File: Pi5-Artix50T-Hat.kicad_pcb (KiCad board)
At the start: 4 copper layers, 65 x 56 mm, 97 parts, among them J1 GPIO, J2 Molex 0878321420, J3 68711614522, U1 FT24C256A, U10 AP62200TWU-7, U11 AP62200TWU-7, U12 AP62200TWU-7, U2 XC7A50T-FGG484, U9 AP62200TWU-7, X1 50MHz

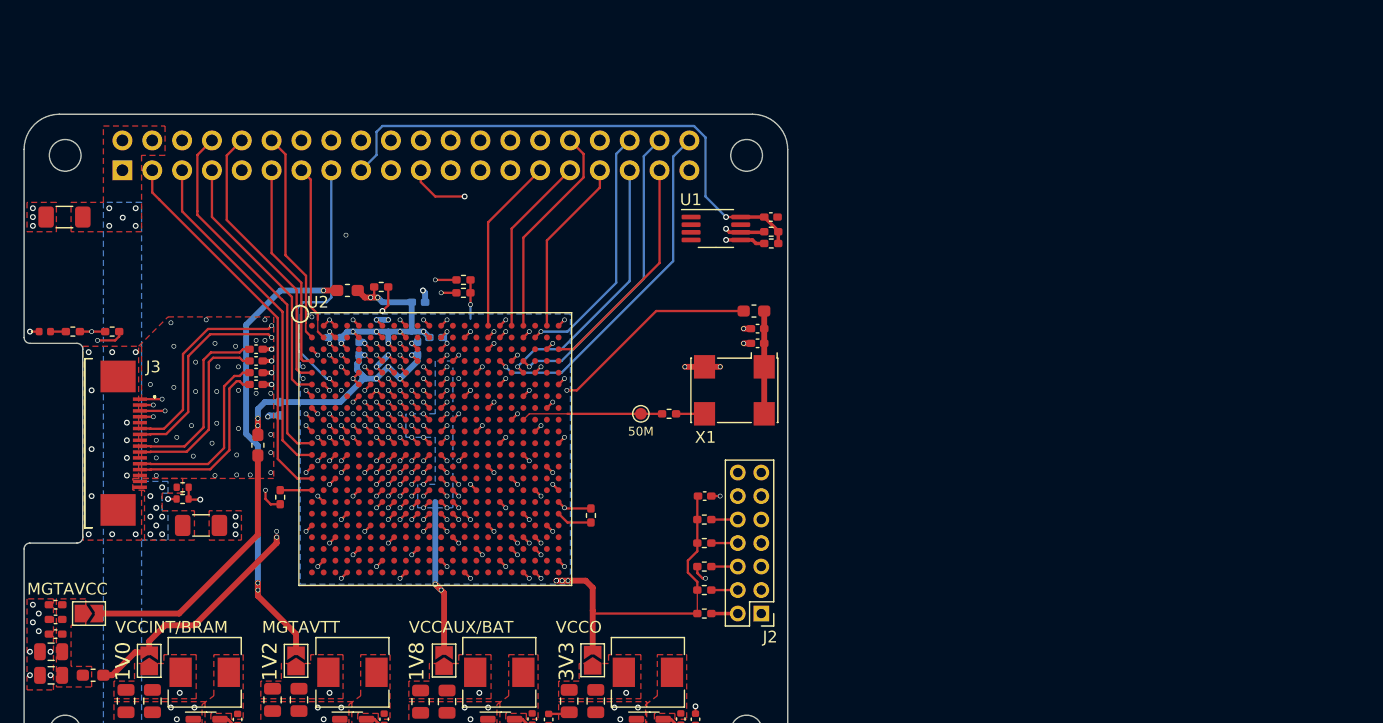
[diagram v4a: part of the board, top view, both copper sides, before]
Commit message: Updated decoupling. Need to work out larger planes and fills.
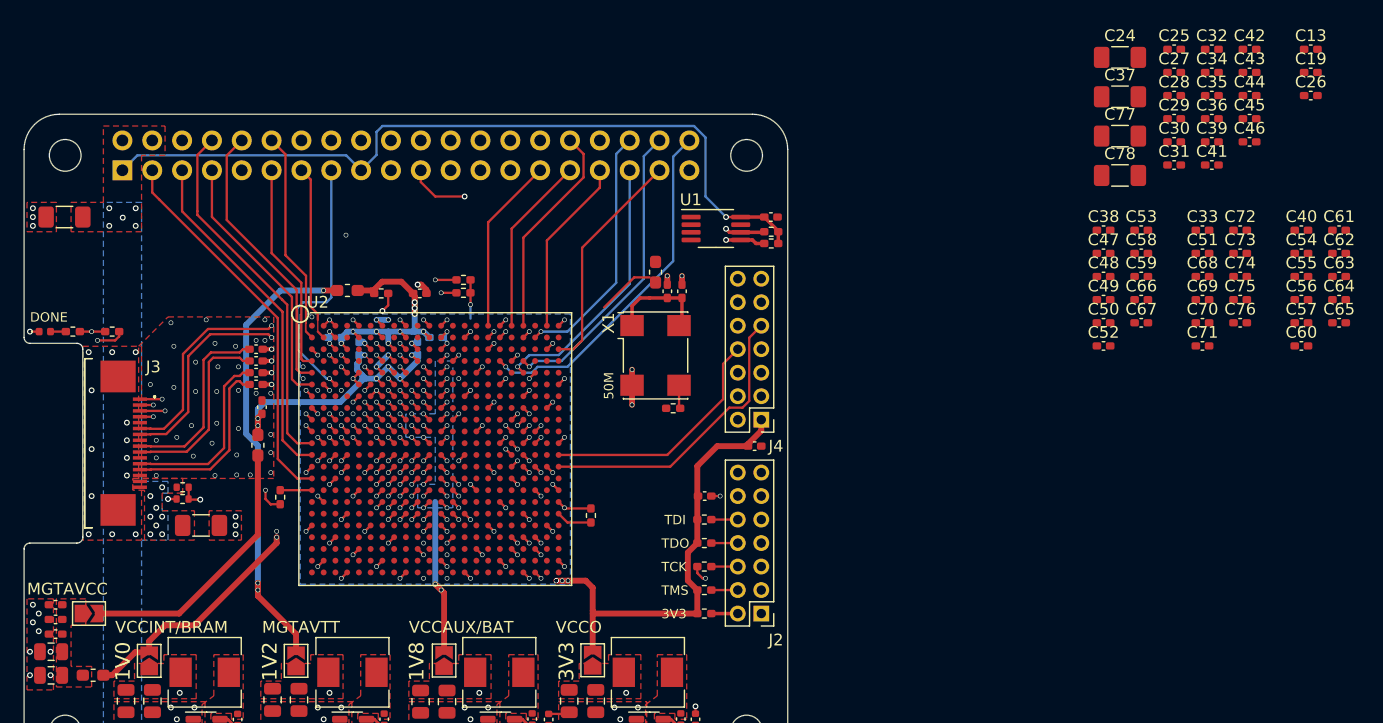
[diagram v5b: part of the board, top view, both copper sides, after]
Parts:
- removed TP1: 50M, TestPoint:TestPoint_Pad_D1.0mm
- added C13: 100n, Capacitor_SMD:C_0402_1005Metric_Pad0.74x0.62mm_HandSolder, F.Cu at (209.5, 38.5)
- added C19: 100n, Capacitor_SMD:C_0402_1005Metric_Pad0.74x0.62mm_HandSolder, F.Cu at (209.5, 40.4)
- added C22: 100n, Capacitor_SMD:C_0402_1005Metric_Pad0.74x0.62mm_HandSolder, F.Cu at (162.2, 72.2)
- added C24: 100u, Capacitor_SMD:C_1206_3216Metric_Pad1.33x1.80mm_HandSolder, F.Cu at (193.3, 39.2)
- added C25: 4.7u, Capacitor_SMD:C_0402_1005Metric_Pad0.74x0.62mm_HandSolder, F.Cu at (197.9, 38.5)
- added C26: 4.7u, Capacitor_SMD:C_0402_1005Metric_Pad0.74x0.62mm_HandSolder, F.Cu at (209.5, 42.4)
- added C27: 4.7u, Capacitor_SMD:C_0402_1005Metric_Pad0.74x0.62mm_HandSolder, F.Cu at (197.9, 40.4)
- added C28: 4.7u, Capacitor_SMD:C_0402_1005Metric_Pad0.74x0.62mm_HandSolder, F.Cu at (197.9, 42.4)
- added C29: 100n, Capacitor_SMD:C_0402_1005Metric_Pad0.74x0.62mm_HandSolder, F.Cu at (197.9, 44.4)
- added C30: 100n, Capacitor_SMD:C_0402_1005Metric_Pad0.74x0.62mm_HandSolder, F.Cu at (197.9, 46.4)
- added C31: 100n, Capacitor_SMD:C_0402_1005Metric_Pad0.74x0.62mm_HandSolder, F.Cu at (197.9, 48.3)
- added C32: 100n, Capacitor_SMD:C_0402_1005Metric_Pad0.74x0.62mm_HandSolder, F.Cu at (201.1, 38.5)
- added C33: 100n, Capacitor_SMD:C_0402_1005Metric_Pad0.74x0.62mm_HandSolder, F.Cu at (200.3, 53.9)
- added C34: 100n, Capacitor_SMD:C_0402_1005Metric_Pad0.74x0.62mm_HandSolder, F.Cu at (201.1, 40.4)
- added C35: 4.7u, Capacitor_SMD:C_0402_1005Metric_Pad0.74x0.62mm_HandSolder, F.Cu at (201.1, 42.4)
- added C36: 100n, Capacitor_SMD:C_0402_1005Metric_Pad0.74x0.62mm_HandSolder, F.Cu at (201.1, 44.4)
- added C37: 100u, Capacitor_SMD:C_1206_3216Metric_Pad1.33x1.80mm_HandSolder, F.Cu at (193.3, 42.5)
- added C38: 100n, Capacitor_SMD:C_0402_1005Metric_Pad0.74x0.62mm_HandSolder, F.Cu at (191.9, 53.9)
- added C39: 4.7u, Capacitor_SMD:C_0402_1005Metric_Pad0.74x0.62mm_HandSolder, F.Cu at (201.1, 46.4)
- added C40: 100n, Capacitor_SMD:C_0402_1005Metric_Pad0.74x0.62mm_HandSolder, F.Cu at (208.7, 53.9)
- added C41: 4.7u, Capacitor_SMD:C_0402_1005Metric_Pad0.74x0.62mm_HandSolder, F.Cu at (201.1, 48.3)
- added C42: 100n, Capacitor_SMD:C_0402_1005Metric_Pad0.74x0.62mm_HandSolder, F.Cu at (204.3, 38.5)
- added C43: 100n, Capacitor_SMD:C_0402_1005Metric_Pad0.74x0.62mm_HandSolder, F.Cu at (204.3, 40.4)
- added C44: 100n, Capacitor_SMD:C_0402_1005Metric_Pad0.74x0.62mm_HandSolder, F.Cu at (204.3, 42.4)
- added C45: 100n, Capacitor_SMD:C_0402_1005Metric_Pad0.74x0.62mm_HandSolder, F.Cu at (204.3, 44.4)
- added C46: 100n, Capacitor_SMD:C_0402_1005Metric_Pad0.74x0.62mm_HandSolder, F.Cu at (204.3, 46.4)
- added C47: 100n, Capacitor_SMD:C_0402_1005Metric_Pad0.74x0.62mm_HandSolder, F.Cu at (191.9, 55.8)
- added C48: 100n, Capacitor_SMD:C_0402_1005Metric_Pad0.74x0.62mm_HandSolder, F.Cu at (191.9, 57.8)
- added C49: 100n, Capacitor_SMD:C_0402_1005Metric_Pad0.74x0.62mm_HandSolder, F.Cu at (191.9, 59.8)
- added C50: 4.7u, Capacitor_SMD:C_0402_1005Metric_Pad0.74x0.62mm_HandSolder, F.Cu at (191.9, 61.8)
- added C51: 100n, Capacitor_SMD:C_0402_1005Metric_Pad0.74x0.62mm_HandSolder, F.Cu at (200.3, 55.8)
- added C52: 100n, Capacitor_SMD:C_0402_1005Metric_Pad0.74x0.62mm_HandSolder, F.Cu at (191.9, 63.7)
- added C53: 100n, Capacitor_SMD:C_0402_1005Metric_Pad0.74x0.62mm_HandSolder, F.Cu at (195.1, 53.9)
- added C54: 4.7u, Capacitor_SMD:C_0402_1005Metric_Pad0.74x0.62mm_HandSolder, F.Cu at (208.7, 55.8)
- added C55: 100n, Capacitor_SMD:C_0402_1005Metric_Pad0.74x0.62mm_HandSolder, F.Cu at (208.7, 57.8)
- added C56: 100n, Capacitor_SMD:C_0402_1005Metric_Pad0.74x0.62mm_HandSolder, F.Cu at (208.7, 59.8)
- added C57: 100n, Capacitor_SMD:C_0402_1005Metric_Pad0.74x0.62mm_HandSolder, F.Cu at (208.7, 61.8)
- added C58: 100n, Capacitor_SMD:C_0402_1005Metric_Pad0.74x0.62mm_HandSolder, F.Cu at (195.1, 55.8)
- added C59: 100n, Capacitor_SMD:C_0402_1005Metric_Pad0.74x0.62mm_HandSolder, F.Cu at (195.1, 57.8)
- added C60: 100n, Capacitor_SMD:C_0402_1005Metric_Pad0.74x0.62mm_HandSolder, F.Cu at (208.7, 63.7)
- added C61: 100n, Capacitor_SMD:C_0402_1005Metric_Pad0.74x0.62mm_HandSolder, F.Cu at (211.9, 53.9)
- added C62: 100n, Capacitor_SMD:C_0402_1005Metric_Pad0.74x0.62mm_HandSolder, F.Cu at (211.9, 55.8)
- added C63: 100n, Capacitor_SMD:C_0402_1005Metric_Pad0.74x0.62mm_HandSolder, F.Cu at (211.9, 57.8)
- added C64: 100n, Capacitor_SMD:C_0402_1005Metric_Pad0.74x0.62mm_HandSolder, F.Cu at (211.9, 59.8)
- added C65: 4.7u, Capacitor_SMD:C_0402_1005Metric_Pad0.74x0.62mm_HandSolder, F.Cu at (211.9, 61.8)
- added C66: 100n, Capacitor_SMD:C_0402_1005Metric_Pad0.74x0.62mm_HandSolder, F.Cu at (195.1, 59.8)
- added C67: 4.7u, Capacitor_SMD:C_0402_1005Metric_Pad0.74x0.62mm_HandSolder, F.Cu at (195.1, 61.8)
- added C68: 100n, Capacitor_SMD:C_0402_1005Metric_Pad0.74x0.62mm_HandSolder, F.Cu at (200.3, 57.8)
- added C69: 100n, Capacitor_SMD:C_0402_1005Metric_Pad0.74x0.62mm_HandSolder, F.Cu at (200.3, 59.8)
- added C70: 4.7u, Capacitor_SMD:C_0402_1005Metric_Pad0.74x0.62mm_HandSolder, F.Cu at (200.3, 61.8)
- added C71: 100n, Capacitor_SMD:C_0402_1005Metric_Pad0.74x0.62mm_HandSolder, F.Cu at (200.3, 63.7)
- added C72: 100n, Capacitor_SMD:C_0402_1005Metric_Pad0.74x0.62mm_HandSolder, F.Cu at (203.5, 53.9)
- added C73: 100n, Capacitor_SMD:C_0402_1005Metric_Pad0.74x0.62mm_HandSolder, F.Cu at (203.5, 55.8)
- added C74: 100n, Capacitor_SMD:C_0402_1005Metric_Pad0.74x0.62mm_HandSolder, F.Cu at (203.5, 57.8)
- added C75: 100n, Capacitor_SMD:C_0402_1005Metric_Pad0.74x0.62mm_HandSolder, F.Cu at (203.5, 59.8)
- added C76: 4.7u, Capacitor_SMD:C_0402_1005Metric_Pad0.74x0.62mm_HandSolder, F.Cu at (203.5, 61.8)
- added C77: 100u, Capacitor_SMD:C_1206_3216Metric_Pad1.33x1.80mm_HandSolder, F.Cu at (193.3, 45.9)
- added C78: 100u, Capacitor_SMD:C_1206_3216Metric_Pad1.33x1.80mm_HandSolder, F.Cu at (193.3, 49.2)
- added J4: Molex 0878321420, Connector_PinHeader_2.00mm:PinHeader_2x07_P2.00mm_Vertical, F.Cu at (162.8, 70.0)
- C10, C15: moved to F.Cu
- moved FB3 9.00 mm to (153.8, 57.4), turned to -90 degrees
- moved C93 8.87 mm to (154.8, 59.1), turned to -90 degrees
- moved X1 7.34 mm to (153.8, 64.5), turned to -90 degrees
- moved C94 7.18 mm to (156.0, 59.1), turned to -90 degrees
- moved C15 1.51 mm to (120.2, 68.9), turned to -90 degrees
- moved C10 0.76 mm to (133.7, 59.2)
- moved R16 0.59 mm to (155.2, 69.0)
- moved R13 0.55 mm to (130.4, 59.2)
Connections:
- U2 pad H19: unconnected-(U2B-IO_L12N_T1_MRCC_15-PadH19) -> /FPGA Top/FPGA Bank 15 & 16/IOHEADER0
- U2 pad K18: unconnected-(U2B-IO_L13P_T2_MRCC_15-PadK18) -> /FPGA Top/FPGA Bank 15 & 16/IOHEADER1
- U2 pad K19: unconnected-(U2B-IO_L13N_T2_MRCC_15-PadK19) -> /FPGA Top/FPGA Bank 15 & 16/IOHEADER2
- U2 pad L18: unconnected-(U2B-IO_L16N_T2_A27_15-PadL18) -> /FPGA Top/FPGA Bank 15 & 16/IOHEADER8
- U2 pad L19: unconnected-(U2B-IO_L14P_T2_SRCC_15-PadL19) -> /FPGA Top/FPGA Bank 15 & 16/IOHEADER3
- U2 pad L20: unconnected-(U2B-IO_L14N_T2_SRCC_15-PadL20) -> /FPGA Top/FPGA Bank 15 & 16/IOHEADER4
- U2 pad M18: unconnected-(U2B-IO_L16P_T2_A28_15-PadM18) -> /FPGA Top/FPGA Bank 15 & 16/IOHEADER7
- U2 pad M22: unconnected-(U2B-IO_L15N_T2_DQS_ADV_B_15-PadM22) -> /FPGA Top/FPGA Bank 15 & 16/IOHEADER6
- U2 pad N18: unconnected-(U2B-IO_L17P_T2_A26_15-PadN18) -> /FPGA Top/FPGA Bank 15 & 16/IOHEADER9
- U2 pad N19: unconnected-(U2B-IO_L17N_T2_A25_15-PadN19) -> /FPGA Top/FPGA Bank 15 & 16/IOHEADER10
- U2 pad N20: unconnected-(U2B-IO_L18P_T2_A24_15-PadN20) -> /FPGA Top/FPGA Bank 15 & 16/IOHEADER11
- U2 pad N22: unconnected-(U2B-IO_L15P_T2_DQS_15-PadN22) -> /FPGA Top/FPGA Bank 15 & 16/IOHEADER5
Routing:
- net /FPGA Top/FPGA Bank 15 & 16/IOHEADER1: track 0.00 -> 29.1 mm, vias 0 -> 1
- net /FPGA Top/FPGA Bank 15 & 16/IOHEADER7: track 0.00 -> 26.0 mm, vias 0 -> 1
- net /FPGA Top/FPGA Bank 15 & 16/IOHEADER5: track 0.00 -> 25.4 mm
- net /FPGA Top/FPGA Bank 15 & 16/IOHEADER3: track 0.00 -> 25.2 mm, vias 0 -> 1
- net /FPGA Top/FPGA Bank 15 & 16/IOHEADER9: track 0.00 -> 24.6 mm, vias 0 -> 1
- net /FPGA Top/FPGA Bank 15 & 16/IOHEADER0: track 0.00 -> 23.2 mm, vias 0 -> 1
- net /FPGA Top/FPGA Bank 15 & 16/IOHEADER2: track 0.00 -> 22.8 mm, vias 0 -> 1
- net /FPGA Top/FPGA Bank 15 & 16/IOHEADER11: track 0.00 -> 22.1 mm, vias 0 -> 1
- net /FPGA Top/FPGA Bank 15 & 16/IOHEADER8: track 0.00 -> 22.1 mm, vias 0 -> 1
- net /FPGA Top/FPGA Bank 15 & 16/IOHEADER4: track 0.00 -> 21.4 mm, vias 0 -> 1
- net +3.3VP: track 45.9 -> 67.3 mm
- net /FPGA Top/FPGA Bank 15 & 16/IOHEADER10: track 0.00 -> 21.1 mm, vias 0 -> 1
- net /FPGA Top/FPGA Bank 15 & 16/IOHEADER6: track 0.00 -> 20.7 mm
- net Net-(X1-EN): track 8.75 -> 13.8 mm
- net /FPGA Top/CLK50MHZ: track 12.0 -> 15.2 mm, vias 0 -> 1
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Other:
- board text added: "50M"
- board text added: "Bottom Copper Fill is 3V3."
- board text added: "DONE"
- board text added: "TCK"
- board text added: "TDI"
- board text added: "TDO"
- board text added: "TMS"

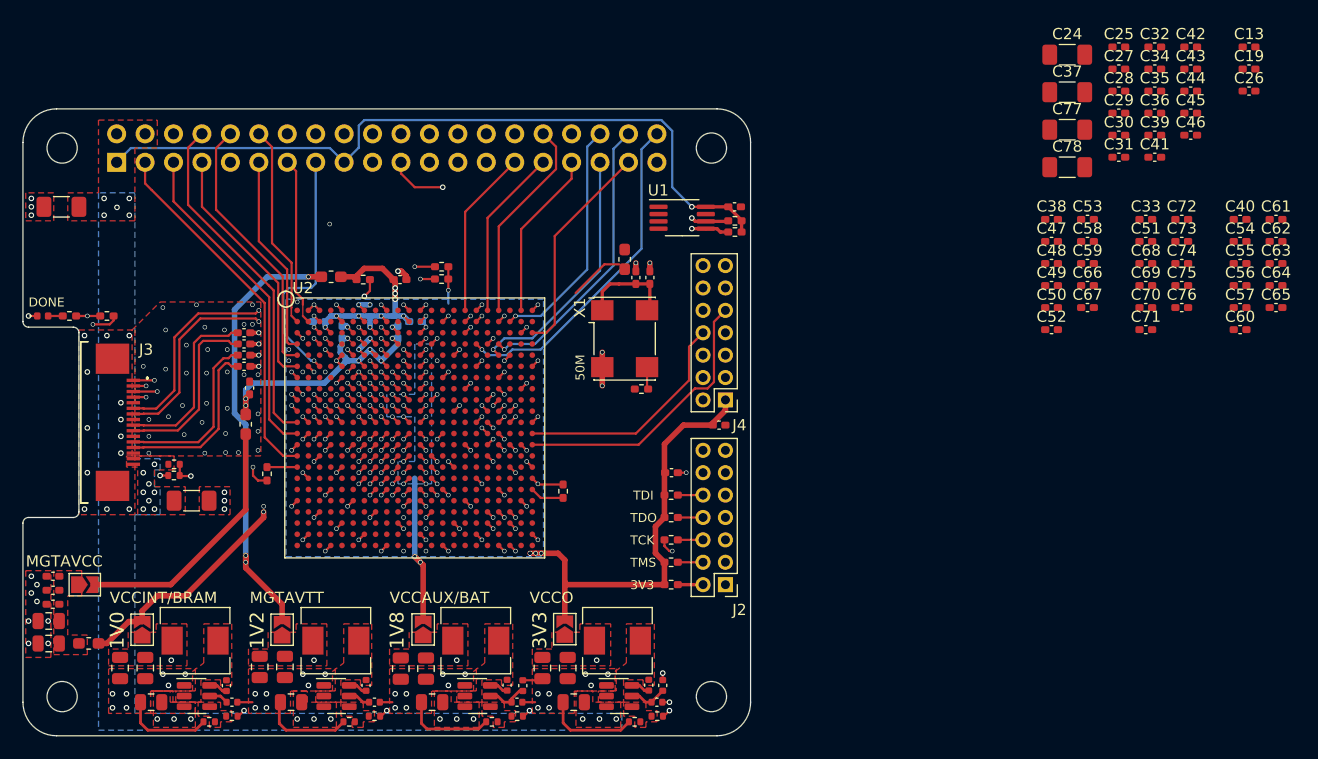
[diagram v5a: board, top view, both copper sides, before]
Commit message: Routing finished; Need to battle through the DRCs now. There's a few!
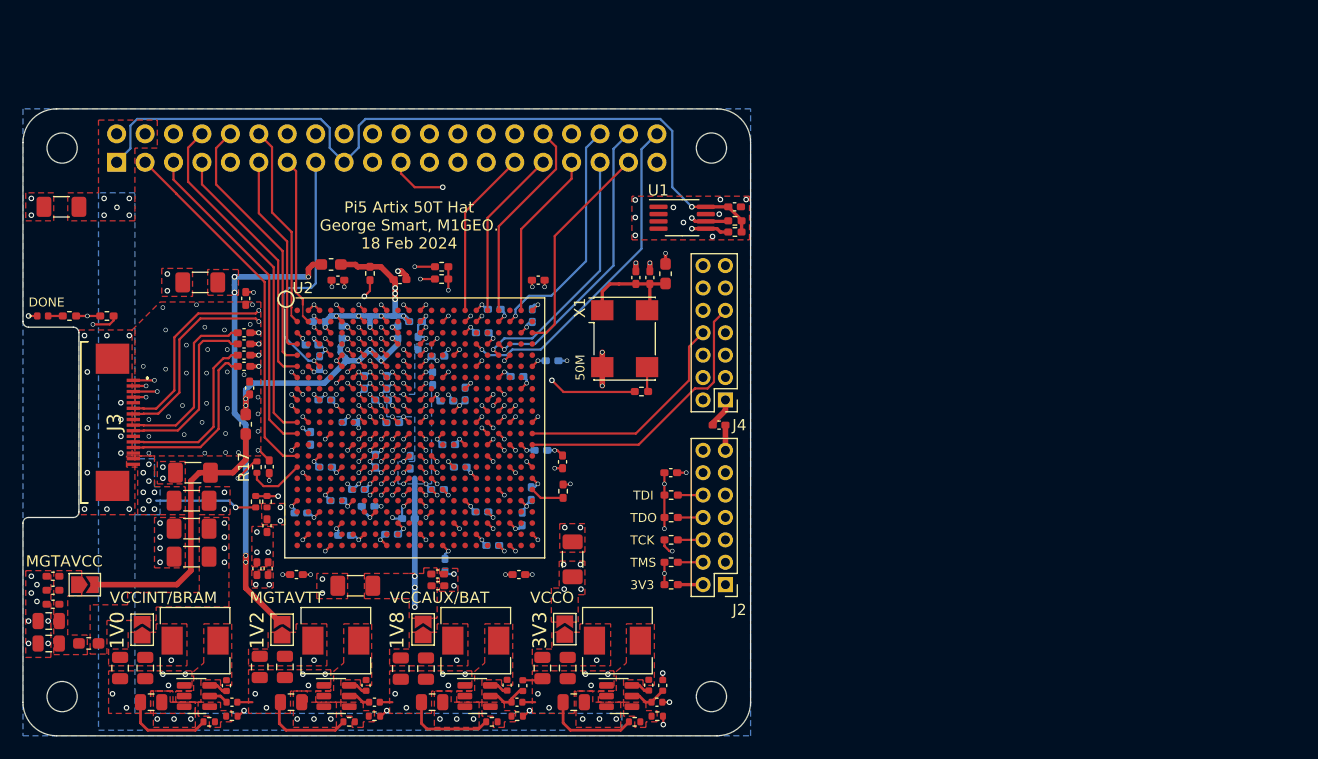
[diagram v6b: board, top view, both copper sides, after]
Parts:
- removed C52, C60, C71: 100n, Capacitor_SMD:C_0402_1005Metric_Pad0.74x0.62mm_HandSolder
- added C23: 100u, Capacitor_SMD:C_1206_3216Metric_Pad1.33x1.80mm_HandSolder, F.Cu at (115.1, 84.0)
- added C79: 100u, Capacitor_SMD:C_1206_3216Metric_Pad1.33x1.80mm_HandSolder, F.Cu at (115.2, 76.5)
- added G***: LOGO, LOGO, B.Cu at (133.4, 92.4)
- C13, C19, C28, C29, C30, C31, C32, C33, C34, C36, C38, C40, C42, C43, C44, C45, C46, C47, C48, C49, C51, C53, C55, C56, C57, C58, C59, C61, C62, C63, C64, C66, C68, C69, C72, C73, C74, C75: moved to B.Cu
- J3: footprint pcie:68711614522 -> 68711614522:68711614522
- R17: footprint Resistor_SMD:R_0402_1005Metric_Pad0.72x0.64mm_HandSolder -> Resistor_SMD:R_0402_1005Metric
- moved C35 90.0 mm to (121.9, 85.1), turned to 90 degrees
- moved C54 89.4 mm to (124.4, 85.6)
- moved C27 89.0 mm to (120.9, 85.1), turned to 90 degrees
- moved C25 87.3 mm to (121.8, 81.2), turned to -90 degrees
- moved C78 84.6 mm to (115.1, 81.5)
- moved C76 82.7 mm to (122.0, 76.0), turned to -90 degrees
- moved C19 81.6 mm to (137.0, 78.0), turned to 180 degrees
- moved C70 80.4 mm to (119.9, 60.9), turned to 90 degrees
- moved C72 80.2 mm to (125.7, 73.4), turned to -90 degrees
- moved C24 80.1 mm to (115.8, 59.5)
- moved C55 79.6 mm to (132.9, 82.0)
- moved C42 78.9 mm to (132.0, 70.0)
- moved C26 78.2 mm to (144.3, 85.6)
- moved C69 78.2 mm to (124.8, 80.1)
- moved C75 77.9 mm to (125.8, 65.1), turned to 180 degrees
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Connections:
- C24 pad 2: +1V0 -> +1V2_MGTAVTT
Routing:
- net GND: track 120.1 -> 158.8 mm, vias 193 -> 217
- net +3V3: track 110.1 -> 78.3 mm, vias 57 -> 64
- net +1V0: track 43.0 -> 19.3 mm, vias 19 -> 26
- net +5V: track 0.00 -> 9.14 mm, vias 25 -> 26
- net /FPGA Top/FPGA Config/5V_SNS: track 22.9 -> 18.1 mm
- net +3.3VP: track 67.3 -> 71.8 mm
- net Net-(X1-EN): track 13.8 -> 10.1 mm
- net +1V2_MGTAVTT: track 39.8 -> 42.5 mm, vias 3 -> 5
- net Net-(U2C-IO_L20P_T3_35): track 2.70 -> 5.05 mm
- net /FPGA Top/FPGA Bank 216 (MGT)/MR: track 8.37 -> 10.6 mm
- net +1V0_MGTAVCC: track 23.2 -> 25.3 mm
- net +1V8: track 18.7 -> 17.1 mm, vias 9 -> 10
- net /Raspberry Pi 5/GPIO8/SPI0.CE0: track 20.0 -> 18.5 mm
- net /FPGA Top/PCIE_PWR_EN: track 17.6 -> 18.7 mm
- net unconnected-(U2C-IO_L19P_T3_35-PadN4): track 0.71 -> 0.00 mm, vias 1 -> 0
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- added copper zone on F.Cu, net +1V0
- added copper zone on F.Cu, net +1V2_MGTAVTT
- added copper zone on F.Cu, net +1V8
- added copper zone on F.Cu, net +3V3
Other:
- board text added: "18 Feb 2024 - Pi5 Artix 50T Hat"
- board text added: "Pi5 Artix 50T Hat George Smart, M1GEO. 18 Feb 2024"
